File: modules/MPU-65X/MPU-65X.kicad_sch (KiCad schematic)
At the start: 9 parts, among them J2 DE9_Socket, U1 6502, U2 28C256, U3 62256, U4 74NC00, U5 W65C51, U6 W65C22, U8 MAX232, Y1 1Mhz

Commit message: added joshua
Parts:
- added C1, C2, C3, C4: 1µF, IMNOTWOPR:C_Rect_P200mil, symbol IMNOTWOPR:C
- added D1: RI, LED_THT:LED_D5.0mm_Horizontal_O1.27mm_Z9.0mm, symbol Device:LED_Dual_Bidirectional
- added D2: DTR, LED_THT:LED_D5.0mm_Horizontal_O1.27mm_Z9.0mm, symbol Device:LED_Dual_Bidirectional
- added D3: DCD, LED_THT:LED_D5.0mm_Horizontal_O1.27mm_Z9.0mm, symbol Device:LED_Dual_Bidirectional
- added D4: DSR, LED_THT:LED_D5.0mm_Horizontal_O1.27mm_Z9.0mm, symbol Device:LED_Dual_Bidirectional
- added D5: RTS, LED_THT:LED_D5.0mm_Horizontal_O1.27mm_Z3.0mm, symbol Device:LED_Dual_Bidirectional
- added D6: RTR, LED_THT:LED_D5.0mm_Horizontal_O1.27mm_Z3.0mm, symbol Device:LED_Dual_Bidirectional
- added D7: CTS, LED_THT:LED_D5.0mm_Horizontal_O1.27mm_Z3.0mm, symbol Device:LED_Dual_Bidirectional
- added D8: T_{X}D, LED_THT:LED_D5.0mm_Horizontal_O1.27mm_Z3.0mm, symbol Device:LED_Dual_Bidirectional
- added D9: R_{X}D, LED_THT:LED_D5.0mm_Horizontal_O1.27mm_Z3.0mm, symbol Device:LED_Dual_Bidirectional
- added R1, R2, R3, R4, R5, R6, R7, R8, R9: 1kΩ, IMNOTWOPR:R_Axial_DIN0207_P400mil, symbol IMNOTWOPR:R
- J2: footprint (none) -> Connector_Dsub:DSUB-9_Socket_Horizontal_P2.77x2.54mm_EdgePinOffset9.40mm
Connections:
- net GND: now also U5.1 (V_{SS}), U8.15 (GND), C1.2, C2.2, D1.1 (KA), D2.1 (KA), D3.1 (KA), D4.1 (KA), D5.1 (KA), D6.1 (KA), D7.1 (KA), D8.1 (KA), D9.1 (KA)
- net VCC: now also U5.15 (V_{DD}), U8.16 (VCC)
- net at U8.1 (C1+): now also C3.1
- net at U8.13 (R1IN): now also J2.3
- net at U8.14 (T1OUT): now also J2.2
- net at U8.2 (VS+): now also C2.1
- net at U8.3 (C1-): now also C3.2
- net at U8.4 (C2+): now also C4.1
- net at U8.5 (C2-): now also C4.2
- net at U8.6 (VS-): now also C1.1
- new net: D4.2 (AK), R4.1
- new net: D5.2 (AK), R2.1
- new net: D8.2 (AK), R8.1
- new net: D7.2 (AK), R7.1
- new net: D9.2 (AK), R9.1
- new net: D2.2 (AK), R6.1
- new net: D1.2 (AK), R1.1
- new net: D6.2 (AK), R3.1
- new net: D3.2 (AK), R5.1
- new net CTS: R7.2
- new net DCD: R5.2
- new net DSR: R4.2
- new net DTR: R6.2
- new net RI: R1.2
- new net RTR: R3.2
- new net RTS: R2.2
- new net R_{X}D: R9.2
- new net T_{X}D: R8.2
- no-connect marks 38 -> 42
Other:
- moved on the sheet: J2, U5

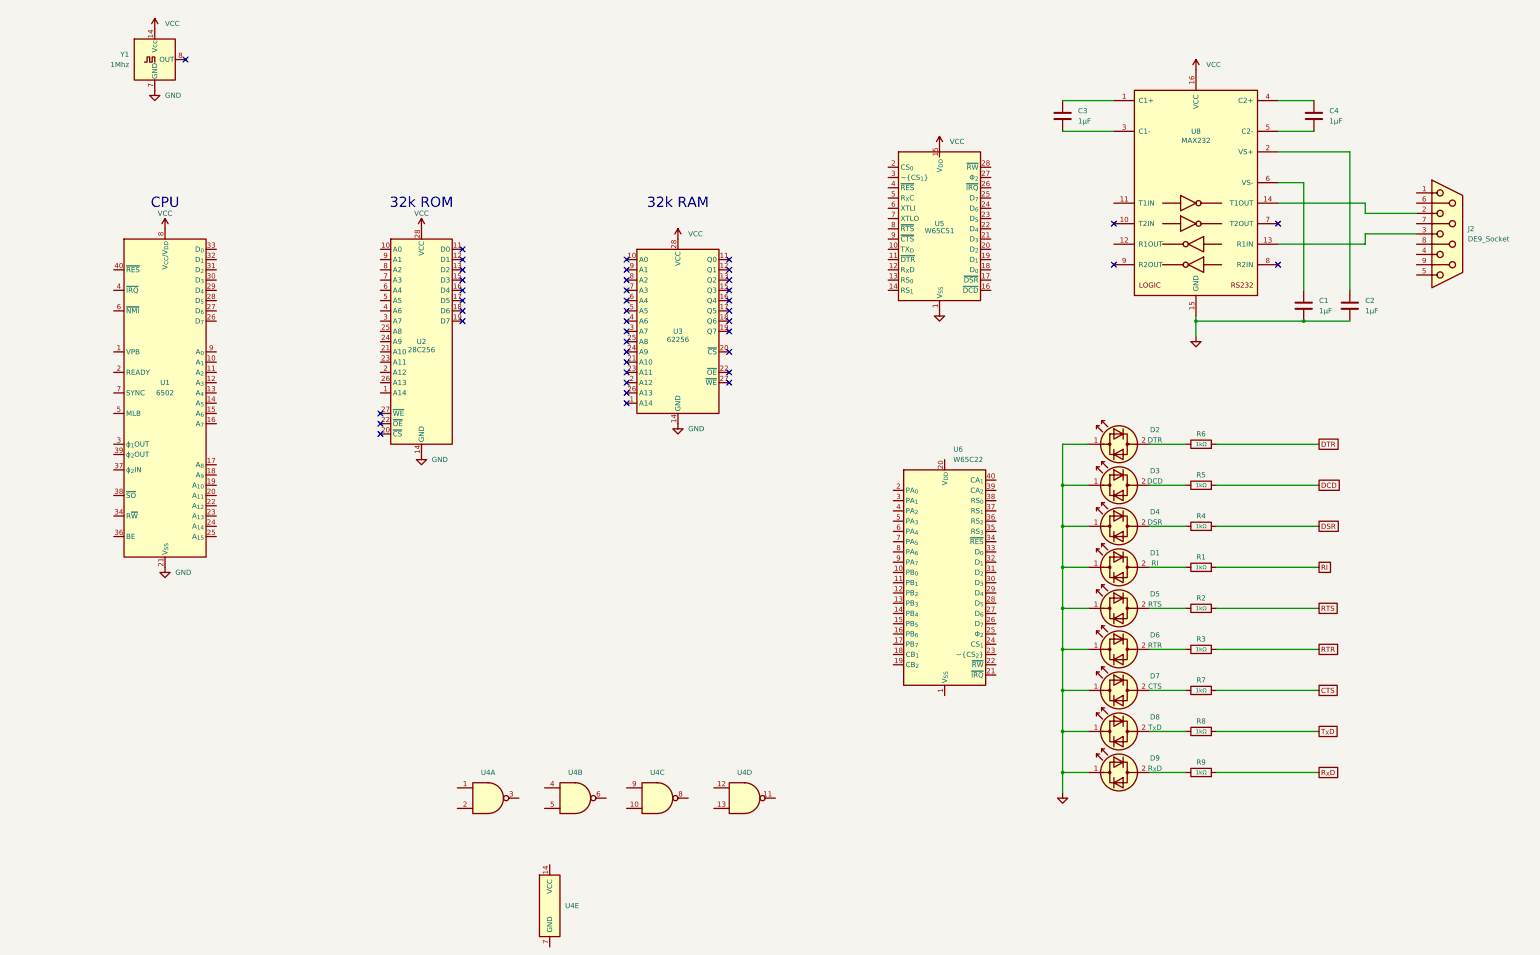
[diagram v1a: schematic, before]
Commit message: mpu-65x circuit & pcb
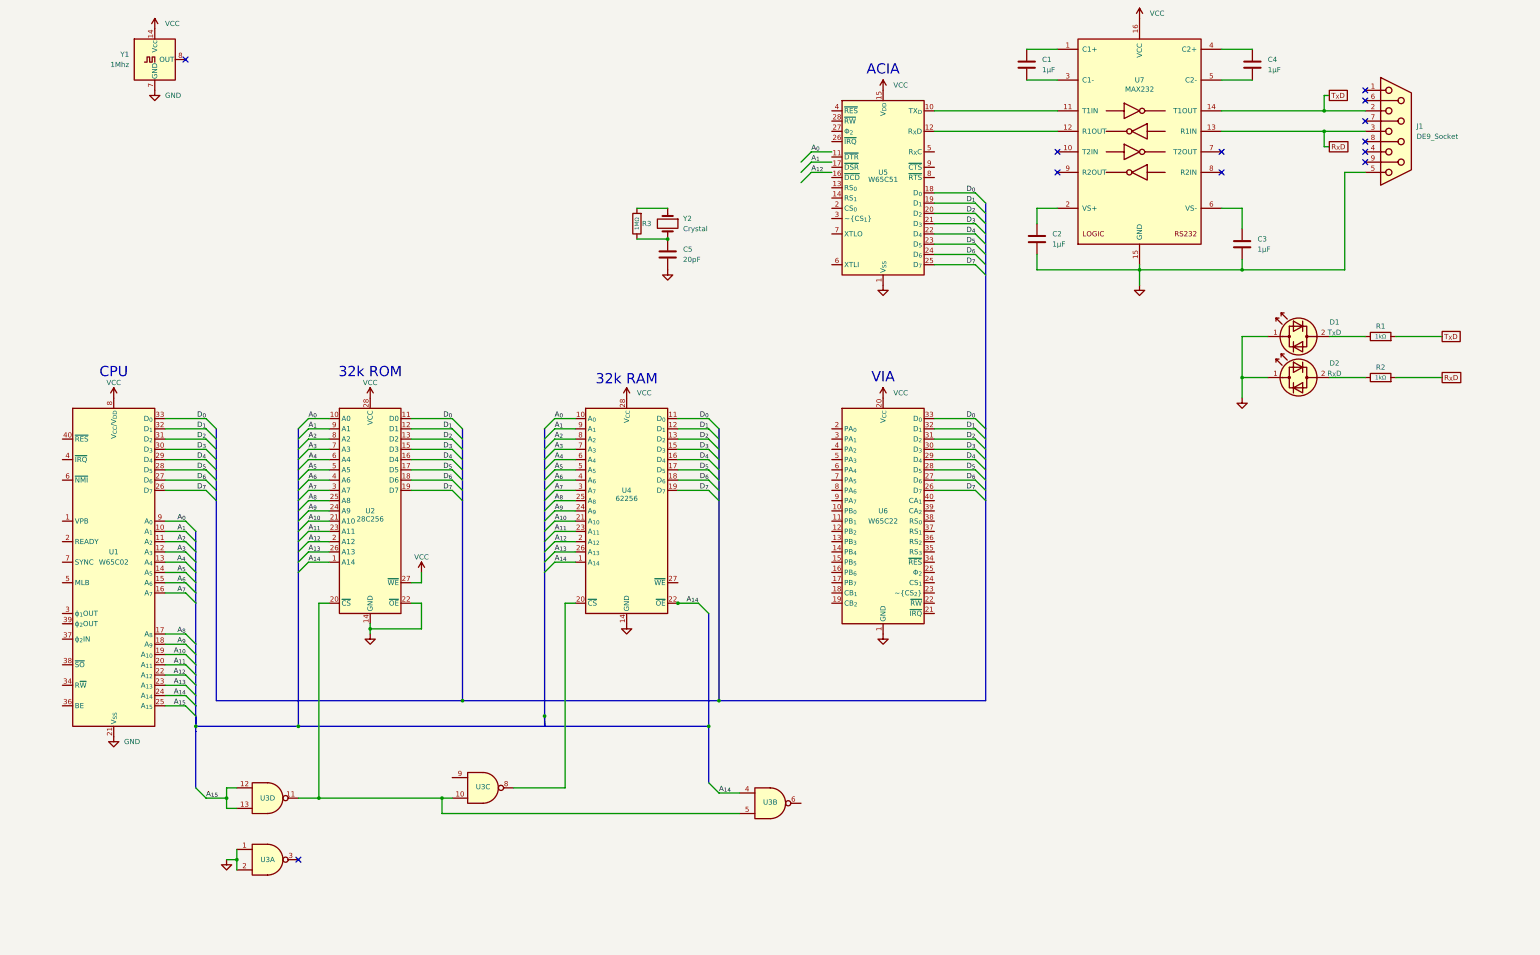
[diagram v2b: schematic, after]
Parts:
- removed D1: RI, LED_THT:LED_D5.0mm_Horizontal_O1.27mm_Z9.0mm, symbol Device:LED_Dual_Bidirectional
- removed D2: DTR, LED_THT:LED_D5.0mm_Horizontal_O1.27mm_Z9.0mm, symbol Device:LED_Dual_Bidirectional
- removed D3: DCD, LED_THT:LED_D5.0mm_Horizontal_O1.27mm_Z9.0mm, symbol Device:LED_Dual_Bidirectional
- removed D4: DSR, LED_THT:LED_D5.0mm_Horizontal_O1.27mm_Z9.0mm, symbol Device:LED_Dual_Bidirectional
- removed D5: RTS, LED_THT:LED_D5.0mm_Horizontal_O1.27mm_Z3.0mm, symbol Device:LED_Dual_Bidirectional
- removed D6: RTR, LED_THT:LED_D5.0mm_Horizontal_O1.27mm_Z3.0mm, symbol Device:LED_Dual_Bidirectional
- removed D7: CTS, LED_THT:LED_D5.0mm_Horizontal_O1.27mm_Z3.0mm, symbol Device:LED_Dual_Bidirectional
- removed R1, R2, R4, R5, R6, R7: 1kΩ, IMNOTWOPR:R_Axial_DIN0207_P400mil, symbol IMNOTWOPR:R
- removed unit 5 of U4
- added C5: 20pF, IMNOTWOPR:C_Rect_P200mil, symbol IMNOTWOPR:C
- added Y2: Crystal, Crystal:Crystal_HC49-U_Horizontal, symbol Device:Crystal
- R3: value 1kΩ -> 1MΩ
- U1: value 6502 -> W65C02; Name (none) -> SOPHRONIA
- U2: footprint (none) -> IMNOTWOPR:ZIF-28W
- U5: Name (none) -> EULALIA
- U6: Name (none) -> MILLICENT
- U7: renamed from U8; Name (none) -> IRIS
- renumbered C3 to C1, C1 to C2, C2 to C3, D8 to D1, D9 to D2, J2 to J1, R8 to R1, R9 to R2, U4 to U3, U3 to U4
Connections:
- net GND: now also J1.5, U2.22 (~{OE}), U3.1, U3.2, U6.1 (GND), C5.2
- net R_{X}D: now also J1.3, U7.13 (R1IN)
- net T_{X}D: now also J1.2, U7.14 (T1OUT)
- net VCC: now also U2.27 (~{WE}), U6.20 (V_{CC})
- net A_{1}: now reaches U1.10 (A_{1})
- net A_{1}: now also U2.9 (A1), U4.9 (A_{1})
- net A_{2}: now reaches U1.11 (A_{2})
- net A_{2}: now also U2.8 (A2), U4.8 (A_{2})
- net A_{3}: now reaches U1.12 (A_{3})
- net A_{3}: now also U2.7 (A3), U4.7 (A_{3})
- net A_{4}: now reaches U1.13 (A_{4})
- net A_{4}: now also U2.6 (A4), U4.6 (A_{4})
- net A_{5}: now reaches U1.14 (A_{5})
- net A_{5}: now also U2.5 (A5), U4.5 (A_{5})
- net A_{6}: now reaches U1.15 (A_{6})
- net A_{6}: now also U2.4 (A6), U4.4 (A_{6})
- net A_{7}: now reaches U1.16 (A_{7})
- net A_{7}: now also U2.3 (A7), U4.3 (A_{7})
- net A_{8}: now reaches U1.17 (A_{8})
- net A_{8}: now also U2.25 (A8), U4.25 (A_{8})
- net A_{9}: now reaches U1.18 (A_{9})
- net A_{9}: now also U2.24 (A9), U4.24 (A_{9})
- net A_{10}: now reaches U1.19 (A_{10})
- net A_{10}: now also U2.21 (A10), U4.21 (A_{10})
- net A_{11}: now reaches U1.20 (A_{11})
- net A_{11}: now also U2.23 (A11), U4.23 (A_{11})
- net A_{12}: now reaches U1.22 (A_{12})
- net A_{12}: now also U2.2 (A12), U4.2 (A_{12})
- net A_{13}: now reaches U1.23 (A_{13})
- net A_{13}: now also U2.26 (A13), U4.26 (A_{13})
- net A_{14}: now reaches U1.24 (A_{14})
- net A_{14}: now also U2.1 (A14), U3.4, U4.1 (A_{14}), U4.22 (~{OE})
- net D_{7}: now reaches U1.26 (D_{7})
- net D_{7}: now also U2.19 (D7), U4.19 (D_{7}), U5.25 (D_{7}), U6.26 (D_{7})
- net D_{6}: now reaches U1.27 (D_{6})
- net D_{6}: now also U2.18 (D6), U4.18 (D_{6}), U5.24 (D_{6}), U6.27 (D_{6})
- net D_{5}: now reaches U1.28 (D_{5})
- net D_{5}: now also U2.17 (D5), U4.17 (D_{5}), U5.23 (D_{5}), U6.28 (D_{5})
- net D_{4}: now reaches U1.29 (D_{4})
- net D_{4}: now also U2.16 (D4), U4.16 (D_{4}), U5.22 (D_{4}), U6.29 (D_{4})
- net D_{3}: now reaches U1.30 (D_{3})
- net D_{3}: now also U2.15 (D3), U4.15 (D_{3}), U5.21 (D_{3}), U6.30 (D_{3})
- net D_{2}: now reaches U1.31 (D_{2})
- net D_{2}: now also U2.13 (D2), U4.13 (D_{2}), U5.20 (D_{2}), U6.31 (D_{2})
- net D_{1}: now reaches U1.32 (D_{1})
- net D_{1}: now also U2.12 (D1), U4.12 (D_{1}), U5.19 (D_{1}), U6.32 (D_{1})
- net D_{0}: now reaches U1.33 (D_{0})
- net D_{0}: now also U2.11 (D0), U4.11 (D_{0}), U5.18 (D_{0}), U6.33 (D_{0})
- net A_{0}: now reaches U1.9 (A_{0})
- net A_{0}: now also U2.10 (A0), U4.10 (A_{0})
- net at C2.1: now also U7.2 (VS+); no longer U7.6 (VS-)
- net at U3.10: now also U2.20 (~{CS}), U3.11, U3.5
- net at U3.8: now also U4.20 (~{CS})
- net at U5.10 (TX_{D}): now also U7.11 (T1IN)
- net at U5.12 (R_{X}D): now also U7.12 (R1OUT)
- net at C3.1: now also U7.6 (VS-); no longer U7.2 (VS+)
- net A_{15}: now reaches U3.12
- net A_{15}: now also U3.13
- net at R3.1: now also C5.1, Y2.2
- net RTR: no longer names the net of R3.2
- net RTR: now also Y2.1
- no-connect marks 42 -> 12
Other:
- note added: "ACIA"
- note added: "VIA"
- moved on the sheet: C1, C2, C3, C4, D1, D2, J1, R1, R2, U1, U2, U3A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

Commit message: Formatting and MPU-65X work
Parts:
- added U8: MAX3243IDBR, IMNOTWOPR:SOP65P780X200-28N, symbol IMNOTWOPR:MAX3243IDBR
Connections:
- net A_{0}: now also U5.13 (RS_{0}), U6.38 (RS_{0})
- net A_{12}: now also U5.2 (CS_{0})
- net A_{13}: now also U6.24 (CS_{1})
- net A_{1}: now also U5.14 (RS_{1}), U6.37 (RS_{1})
- net A_{2}: now also U6.36 (RS_{2})
- net A_{3}: now also U6.35 (RS_{3})
- net at C5.1, R3.1, Y2.2: now also U5.6 (XTLI)
- net at R3.2, Y2.1: now also U5.7 (XTLO)
- net ~{RESET}: now reaches U1.40 (~{RES})
- net ~{RESET}: now also U5.4 (~{RES}), U6.34 (~{RES})
- net at U6.23 (~{CS_{2}}): now also U3.6
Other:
- moved on the sheet: C5, D1, D2, R1, R2, R3, Y2
